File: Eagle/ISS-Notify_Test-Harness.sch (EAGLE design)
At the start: 31 parts, among them U1 ATMEGA32U4, U3 TPS63001, X1 8 MHz

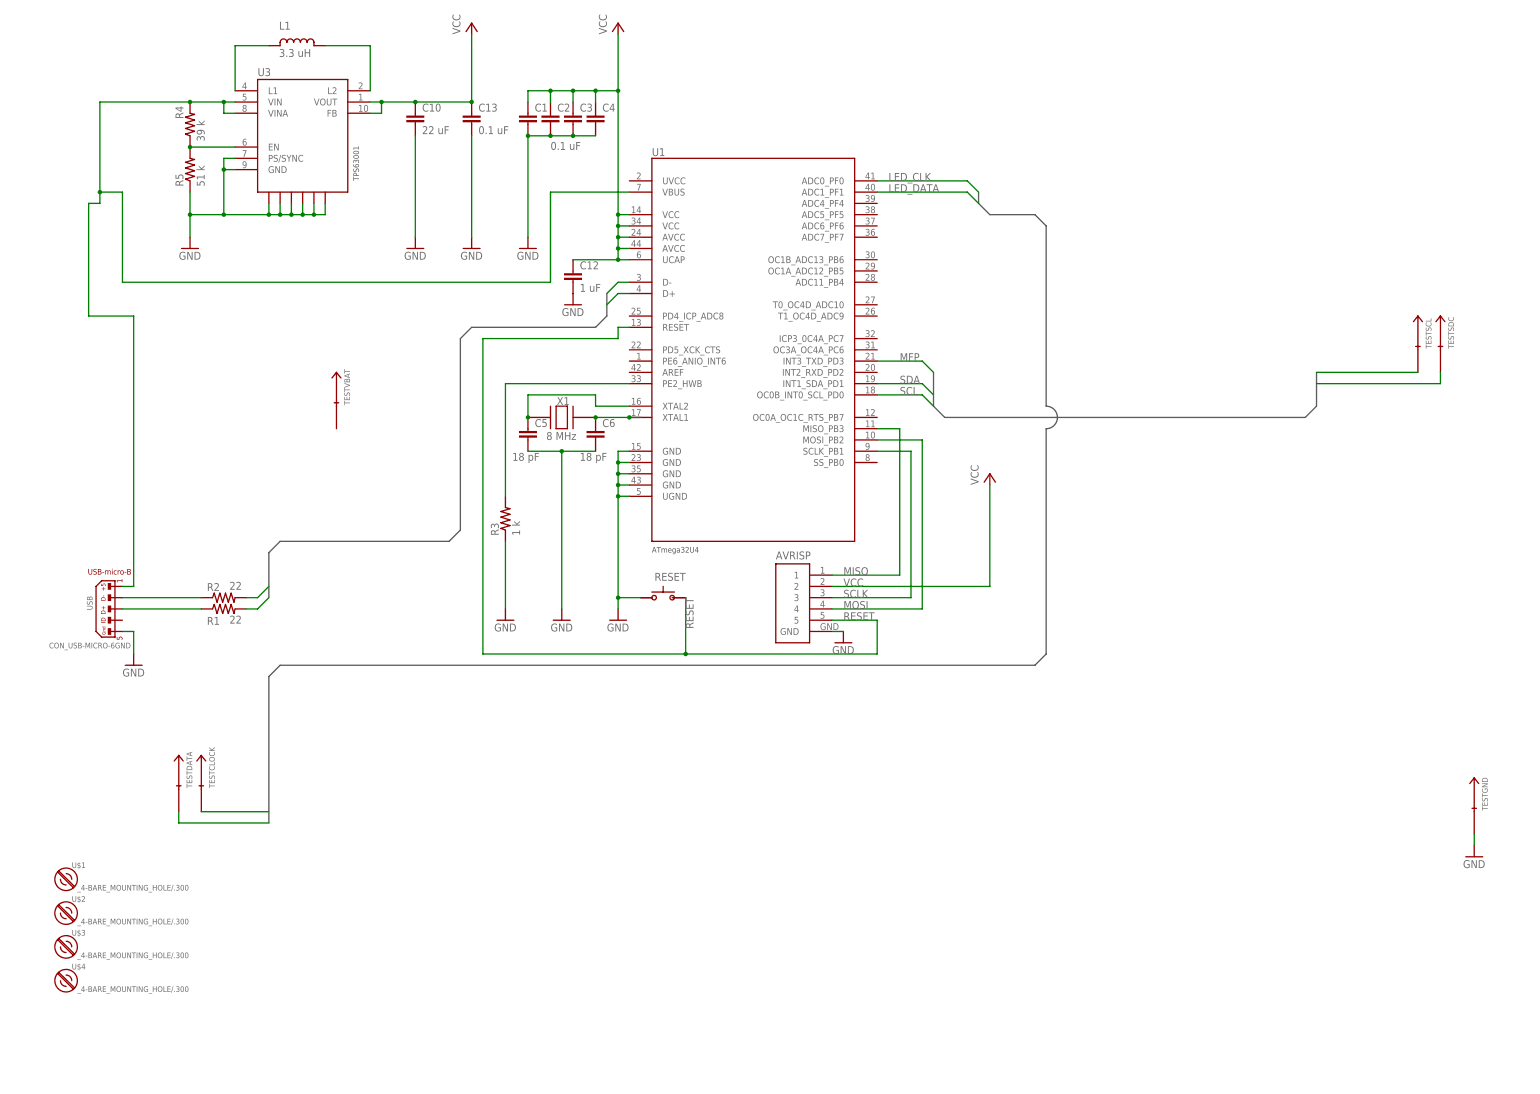
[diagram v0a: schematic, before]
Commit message: pogo pin landings for test harness
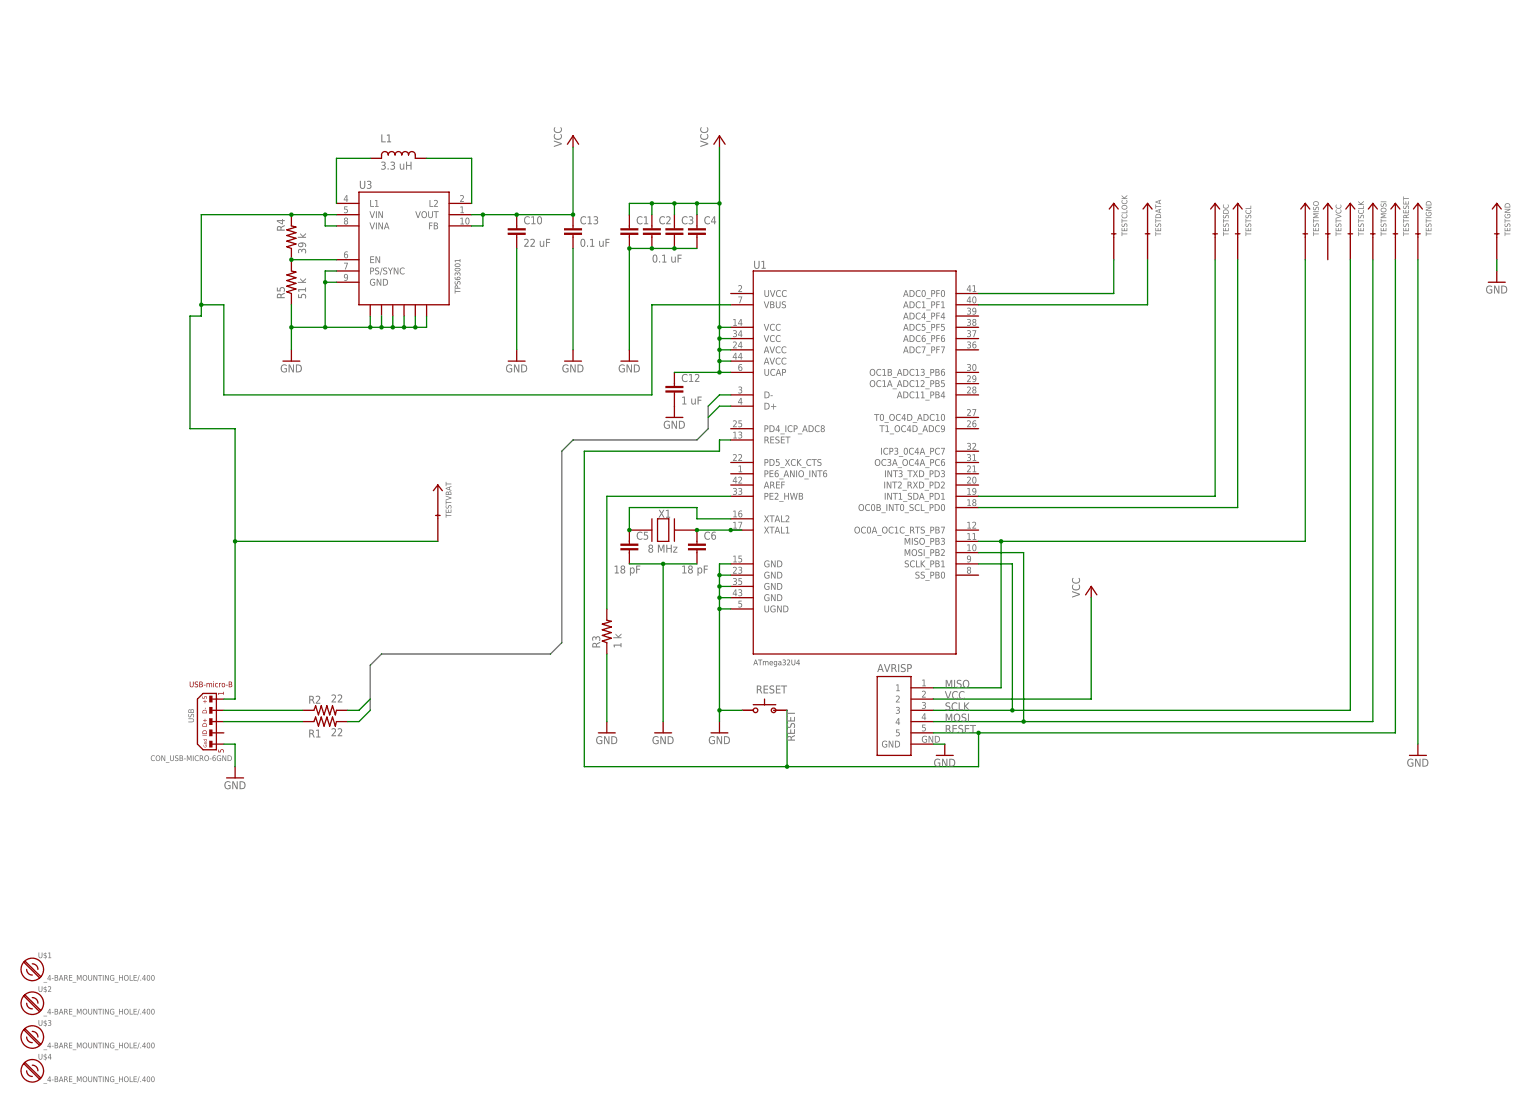
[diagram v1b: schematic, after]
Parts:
- added TESTIGND, TESTMISO, TESTMOSI, TESTRESET, TESTSCLK, TESTVCC: POGOPIN, ISS-Notify:POGOPIN
- TESTCLOCK, TESTDATA, TESTGND, TESTSCL, TESTSDC, TESTVBAT: value TESTPIN -> POGOPIN; device ISS-Notify:TESTPIN -> ISS-Notify:POGOPIN
- U$1, U$2, U$3, U$4: value _4-BARE_MOUNTING_HOLE/.300 -> _4-BARE_MOUNTING_HOLE/.400; device ISS-Notify:_4-BARE_MOUNTING_HOLE/.300 -> ISS-Notify:_4-BARE_MOUNTING_HOLE/.400
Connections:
- removed net MFP: U1.INT3_TXD_PD3
- net GND: now also TESTIGND.TEST
- net MISO: now also TESTMISO.TEST
- net MOSI: now also TESTMOSI.TEST
- net RESET: now also TESTRESET.TEST
- net SCLK: now also TESTSCLK.TEST
- net VIN: now also TESTVBAT.TEST
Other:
- moved on the sheet: AVRISP, C1, C10, C12, C13, C2, C3, C4, C5, C6, L1, R1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

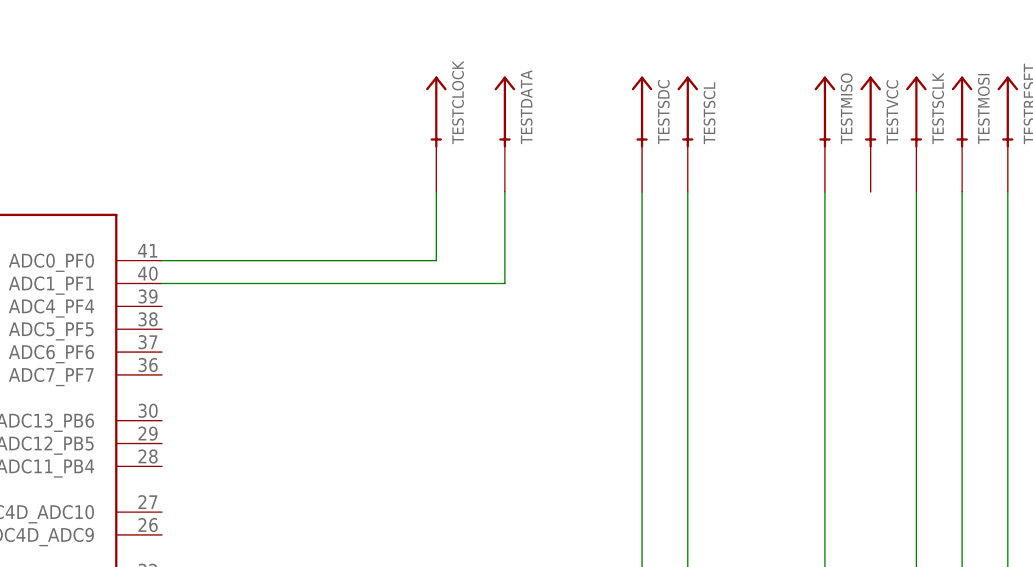
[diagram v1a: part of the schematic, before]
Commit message: first pass routing to pogo pins on test harness
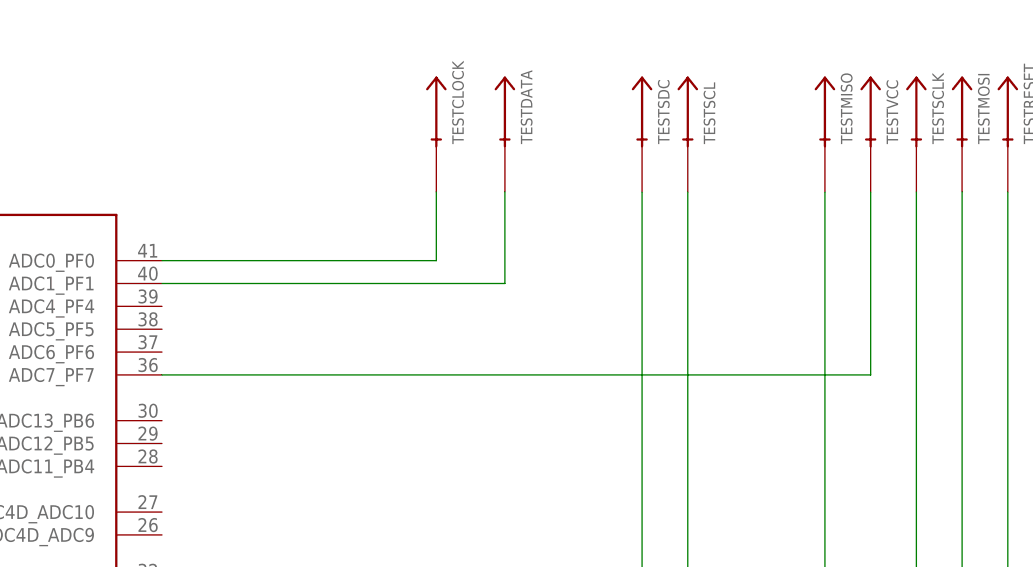
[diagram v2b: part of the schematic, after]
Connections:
- new net N$3: TESTVCC.TEST, U1.ADC7_PF7
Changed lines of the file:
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@@
+</segment>
+</net>
+<net name="N$3" class="0">
+<segment>
+<pinref part="U1" gate="ATMEGA" pin="ADC7_PF7"/>
+<pinref part="TESTVCC" gate="G$1" pin="TEST"/>
+<wire x1="228.6" y1="177.8" x2="307.34" y2="177.8" width="0.1524" layer="91"/>
+<wire x1="307.34" y1="177.8" x2="307.34" y2="198.12" width="0.1524" layer="91"/>
 </segment>
 </net>

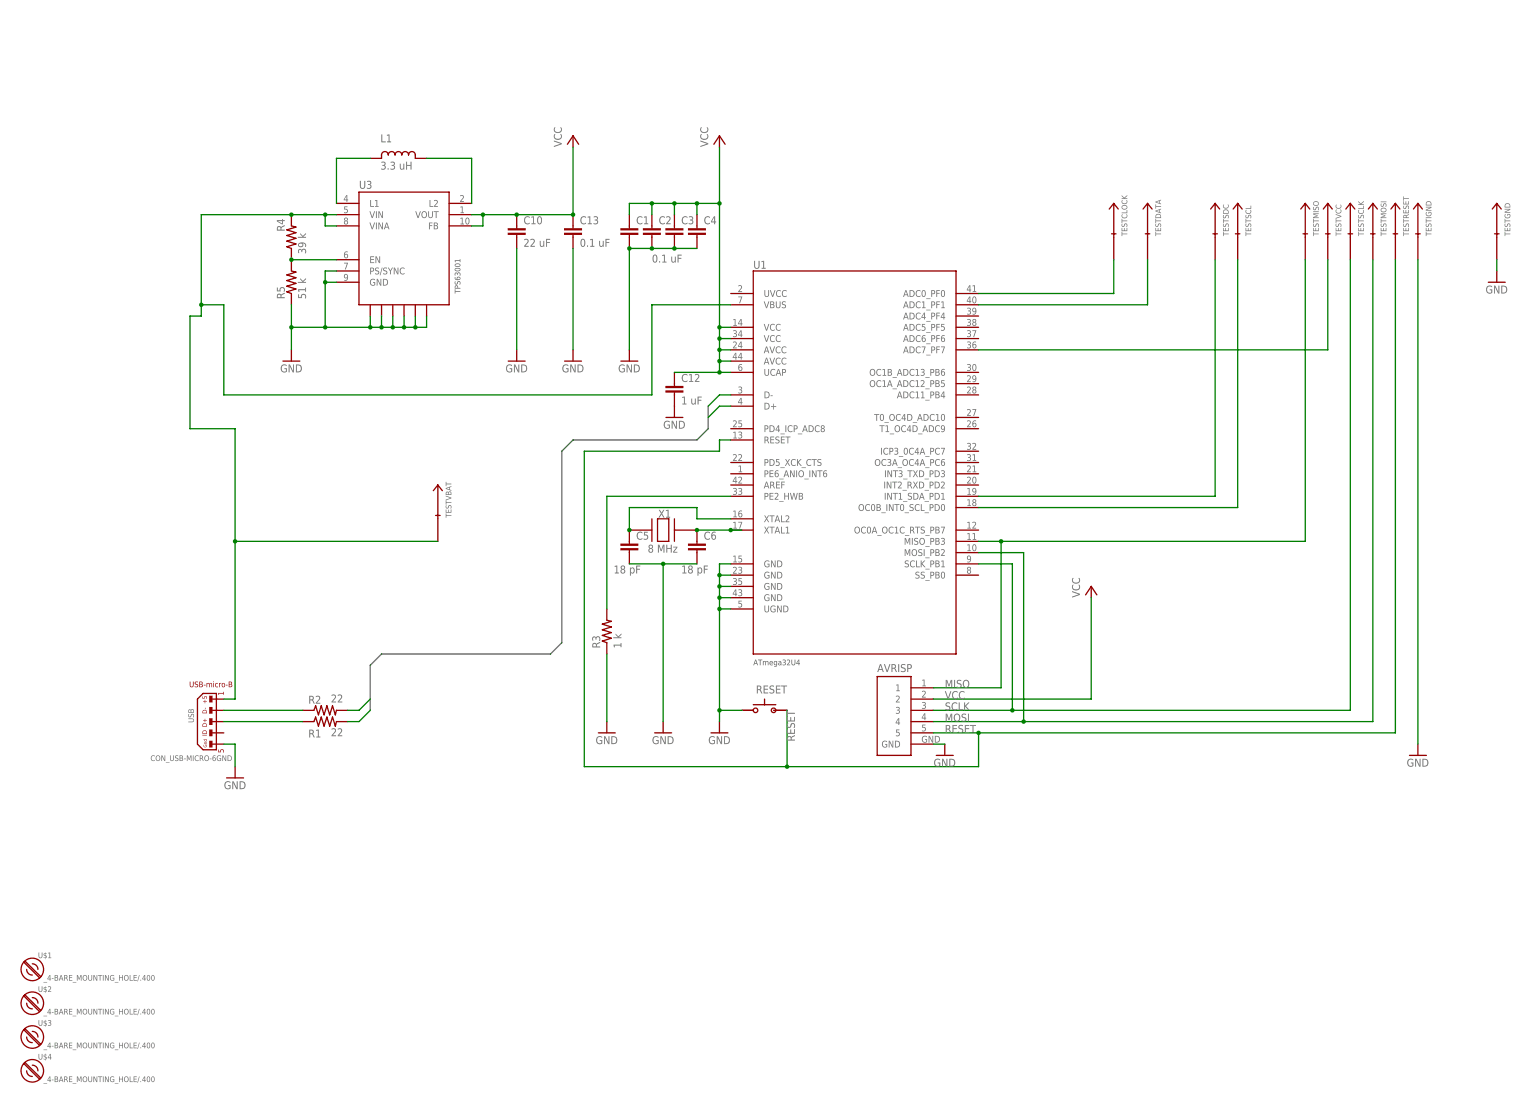
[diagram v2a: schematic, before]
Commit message: clean up power supply, 6 pin header for programming test board
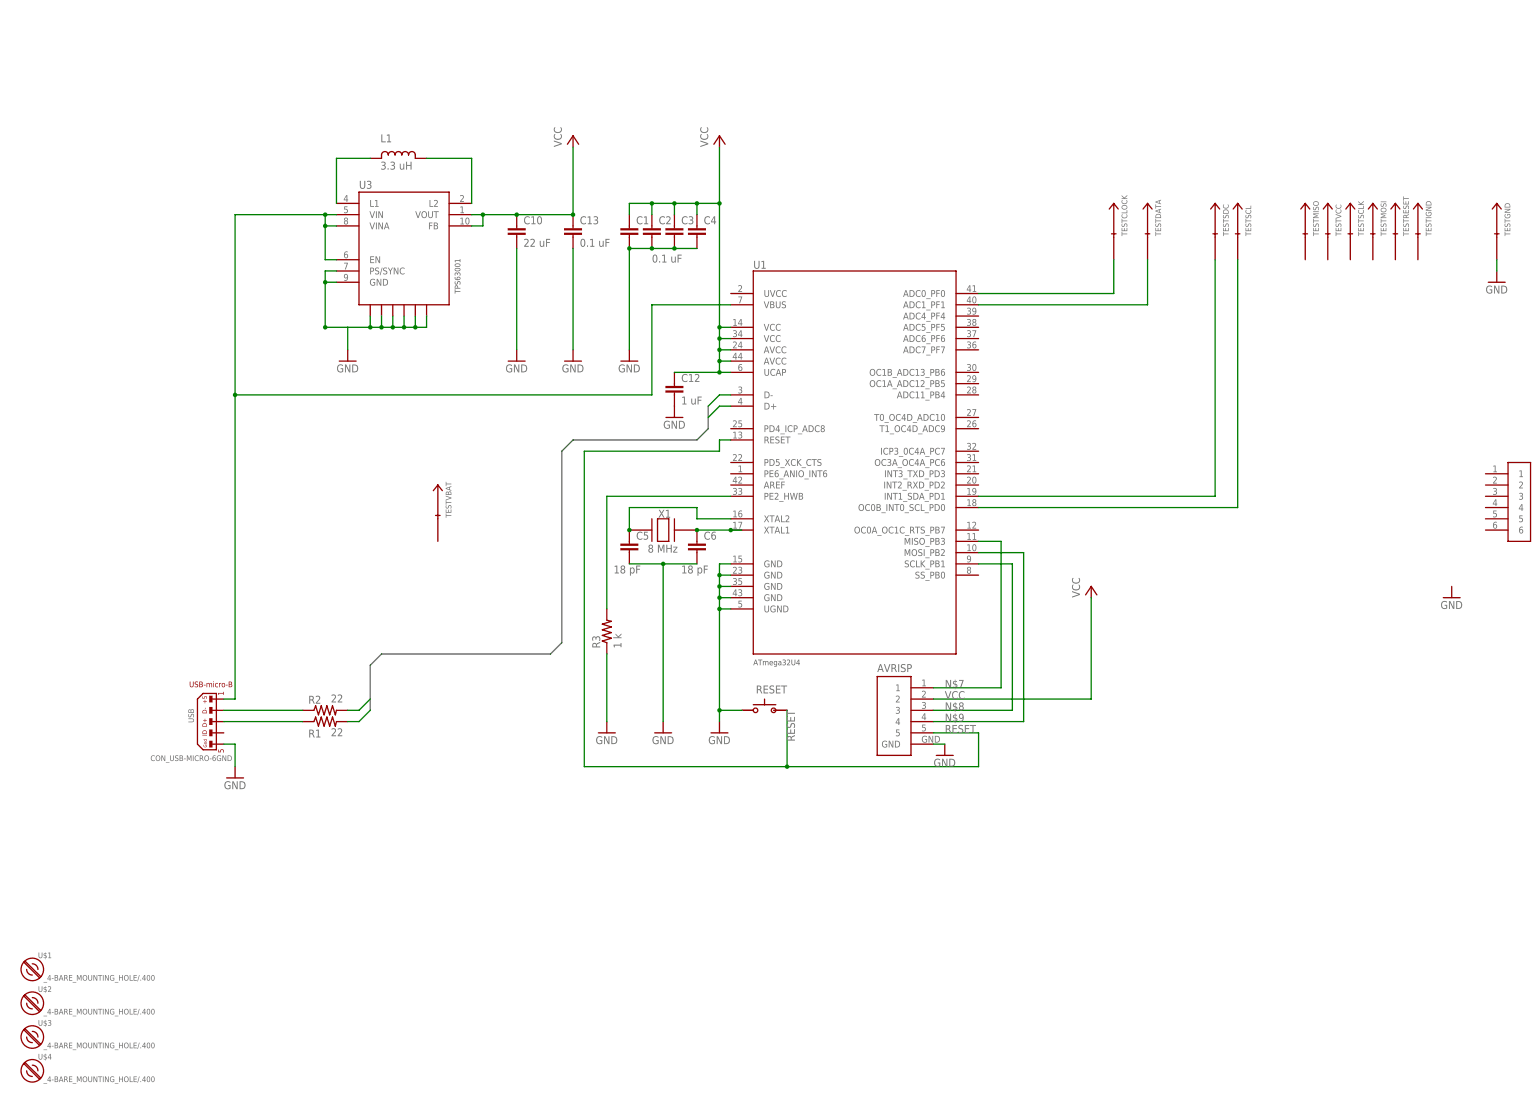
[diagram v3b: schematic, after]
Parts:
- removed R4: 39 k, rcl_custom:R-US_0603-C-NOSILK
- removed R5: 51 k, rcl_custom:R-US_0603-C-NOSILK
- added J1: 6HEADER, ISS-Notify:6HEADER
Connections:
- removed net BATSENSE: R4.1, R5.2, U3.EN
- removed net MISO: AVRISP.1, TESTMISO.TEST, U1.MISO_PB3
- removed net MOSI: AVRISP.4, TESTMOSI.TEST, U1.MOSI_PB2
- removed net N$3: TESTVCC.TEST, U1.ADC7_PF7
- removed net SCLK: AVRISP.3, TESTSCLK.TEST, U1.SCLK_PB1
- new net N$7: AVRISP.1, U1.MISO_PB3
- new net N$8: AVRISP.3, U1.SCLK_PB1
- new net N$9: AVRISP.4, U1.MOSI_PB2
- net GND: no longer R5.1, TESTIGND.TEST
- net RESET: no longer TESTRESET.TEST
- net VIN: now also U3.EN; no longer R4.2, TESTVBAT.TEST
